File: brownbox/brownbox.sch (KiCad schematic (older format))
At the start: 341 parts, among them J1 Rifle Connector - C7-205, J2 12-Pin Cinch Jones Expansion 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, J3 Jumper, Q1 2N5134, Q10 2N5134, Q11 2N5133, Q12 2N5134, Q13 2N5134, Q14 2N5134, Q15 2N5133, Q16 2N5134, Q17 2N5134, Q18 2N5134, Q19 2N5133, Q2 2N5139, Q20 2N5134, Q21 2N5133, Q22 2N5139, Q23 2N5133, Q24 2N5139, Q25 2N5133, Q26 2N5139, Q27 2N5133, Q28 2N5139, Q29 2N5134, Q3 2N5134, Q30 2N5134, Q31 2N5133, Q32 2N5133, Q33 2N5133, Q34 2N5133, Q35 2N5134, Q36 2N5134, Q37 2N5133, Q38 2N5133, Q39 2N5133, Q4 2N5139, Q40 2N5139, Q41 2N5139, Q42 2N5133, Q43 2N5139, Q44 2N5133, Q45 2N5133, Q46 2N5133, Q5 2N5134, Q6 2N5134, Q7 2N5133, Q8 2N5134, Q9 2N5134, T1 CF104 core, #22 wire, X1 3.579545Mhz

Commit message: More small fixes
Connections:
- net S12A1 is gone; now on net VCC: S12.A1
- net S8B3 is gone; now on net S8C3: S8.C3
- net D: now also S15.B2
- net S15C2: now also S15.C2
- net S15D2: now also S15.D2
- net S16A1: no longer S16.B1
- net S16A2: no longer S16.B2
- net S16B1: now also S16.B1
- net S16B2: now also S16.B2
- net S10A1: no longer names the net of S10.A1
- net S10A2: no longer names the net of S10.A2
- net S10A3: no longer names the net of S10.A3
- net S12A2: no longer names the net of S12.A2
- net S5A2: no longer names the net of S5.A2
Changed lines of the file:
@@
 Text GLabel 15450 10850 0    50   Input ~ 0
 S4A1
-Text GLabel 17200 10750 2    50   Input ~ 0
-S5A2
-Wire Wire Line
-	17200 10750 17100 10750
 Text GLabel 19600 10750 2    50   Input ~ 0
 S7A2
@@
 Wire Wire Line
 	12400 12700 12300 12700
-Text GLabel 13600 12700 2    50   Input ~ 0
-S10A2
-Wire Wire Line
-	13600 12700 13500 12700
-Text GLabel 13600 12900 2    50   Input ~ 0
-S10A3
-Wire Wire Line
-	13600 12900 13500 12900
-Text GLabel 13050 12800 0    50   Input ~ 0
-S10A1
-Wire Wire Line
-	13050 12800 13100 12800
-Wire Wire Line
-	14800 12700 14700 12700
 Text GLabel 14800 12900 2    50   Input ~ 0
 S11A3
 Wire Wire Line
 	14800 12900 14700 12900
-Text GLabel 16000 12700 2    50   Input ~ 0
-S12A2
-Wire Wire Line
-	16000 12700 15900 12700
 Text GLabel 16000 12900 2    50   Input ~ 0
 S12A3
 Wire Wire Line
 	16000 12900 15900 12900
-Text GLabel 15450 12800 0    50   Input ~ 0
-S12A1
-Wire Wire Line
-	15450 12800 15500 12800
 Text GLabel 19600 12700 2    50   Input ~ 0
 S15A2
@@
 	20750 10950 20700 10950
 Text GLabel 20800 11750 2    50   Input ~ 0
-S8B3
+S8C3
 Wire Wire Line
 	20800 11750 20700 11750
@@
 S16B3
 Text GLabel 20250 13200 0    50   Input ~ 0
-S16A1
+S16B1
 Wire Wire Line
 	20250 13200 20300 13200
@@
 	20800 13300 20700 13300
 Text GLabel 20800 13100 2    50   Input ~ 0
-S16A2
+S16B2
 Wire Wire Line
 	20800 13100 20700 13100
@@
 	-1   0    0    1
 $EndComp
+$Comp
+L power:VCC #PWR0204
+U 1 1 60BBF6BF
+P 15200 12750
+F 0 "#PWR0204" H 15200 12600 50  0001 C CNN
+F 1 "VCC" H 15215 12923 50  0000 C CNN
+F 2 "" H 15200 12750 50  0001 C CNN
+F 3 "" H 15200 12750 50  0001 C CNN
+	1    15200 12750
+	-1   0    0    -1
+$EndComp
+Wire Wire Line
+	15200 12750 15200 12800
+Wire Wire Line
+	15200 12800 15500 12800
+Wire Wire Line
+	19600 13500 19500 13500
+Wire Wire Line
+	19600 13100 19500 13100
+Wire Wire Line
+	19600 13900 19500 13900
 $EndSCHEMATC

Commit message: Placed NCs, more fixes, Electrical Rules Check makes sense now
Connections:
- net F': now also S9.C2
- net S7B1: no longer RV4.2, RV4.3
- net S9B1: now reaches S9.B1
- net S9B1: now also RV4.2, RV4.3
- net S4A1: no longer names the net of S2.B2, S4.A1
- no-connect marks 0 -> 113
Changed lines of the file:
@@
 S7A2
 Text GLabel 10200 3000 2    50   Input ~ 0
-S7B1
+S9B1
 Wire Wire Line
 	10200 3000 10100 3000
@@
 	7350 15750 7250 15750
 Wire Wire Line
-	7650 15750 7700 15750
-Wire Wire Line
 	9350 14650 9350 14750
 $Comp
@@
 Wire Wire Line
 	16000 10950 15900 10950
-Text GLabel 15450 10850 0    50   Input ~ 0
-S4A1
 Text GLabel 19600 10750 2    50   Input ~ 0
 S7A2
@@
 	13500 12150 13600 12150
 Wire Wire Line
-	15450 10850 15500 10850
-Connection ~ 15500 10850
-Wire Wire Line
 	13550 11850 16350 11850
 Wire Wire Line
@@
 Wire Wire Line
 	19600 13900 19500 13900
+NoConn ~ 13100 14000
+NoConn ~ 13500 13900
+NoConn ~ 13500 14100
+NoConn ~ 13500 13700
+NoConn ~ 13500 13500
+NoConn ~ 13500 13300
+NoConn ~ 13500 13100
+NoConn ~ 13500 12900
+NoConn ~ 13500 12700
+NoConn ~ 13100 12800
+NoConn ~ 13100 13200
+NoConn ~ 13100 13600
+NoConn ~ 11900 11650
+NoConn ~ 12300 11550
+NoConn ~ 12300 11750
+NoConn ~ 12300 11950
+NoConn ~ 12300 12150
+NoConn ~ 11900 12050
+NoConn ~ 14700 11550
+NoConn ~ 14700 11350
+NoConn ~ 14300 11650
+NoConn ~ 14700 11750
+NoConn ~ 14700 11950
+NoConn ~ 14300 12050
+NoConn ~ 14700 12150
+NoConn ~ 15900 11150
+NoConn ~ 15900 11350
+NoConn ~ 15500 11250
+NoConn ~ 15900 11550
+NoConn ~ 15500 11650
+NoConn ~ 15900 11750
+NoConn ~ 15900 11950
+NoConn ~ 15500 12050
+NoConn ~ 15900 12150
+NoConn ~ 16700 11250
+NoConn ~ 17100 11150
+NoConn ~ 17100 11350
+NoConn ~ 17100 11550
+NoConn ~ 17100 11750
+NoConn ~ 16700 11650
+NoConn ~ 17100 11950
+NoConn ~ 17100 12150
+NoConn ~ 16700 12050
+NoConn ~ 18300 11150
+NoConn ~ 18300 11350
+NoConn ~ 17900 11250
+NoConn ~ 18300 11550
+NoConn ~ 18300 11750
+NoConn ~ 17900 11650
+NoConn ~ 18300 12150
+NoConn ~ 17900 12050
+NoConn ~ 19500 11550
+NoConn ~ 19500 11750
+NoConn ~ 19100 11650
+NoConn ~ 19500 11950
+NoConn ~ 19500 12150
+NoConn ~ 19100 12050
+NoConn ~ 20700 11950
+NoConn ~ 20700 12150
+NoConn ~ 20300 12050
+NoConn ~ 12300 12900
+NoConn ~ 12300 13900
+NoConn ~ 14700 13100
+NoConn ~ 15900 13300
+NoConn ~ 15900 13100
+NoConn ~ 15500 13200
+NoConn ~ 15900 13500
+NoConn ~ 15900 13700
+NoConn ~ 15500 13600
+NoConn ~ 15900 13900
+NoConn ~ 15900 14100
+NoConn ~ 15500 14000
+NoConn ~ 15900 12700
+NoConn ~ 17100 12700
+NoConn ~ 17100 12900
+NoConn ~ 17100 13100
+NoConn ~ 17100 13300
+NoConn ~ 17100 13500
+NoConn ~ 17100 13700
+NoConn ~ 17100 13900
+NoConn ~ 17100 14100
+NoConn ~ 16700 14000
+NoConn ~ 16700 13600
+NoConn ~ 16700 13200
+NoConn ~ 16700 12800
+NoConn ~ 18300 12700
+NoConn ~ 18300 12900
+NoConn ~ 18300 11950
+Wire Wire Line
+	7650 15750 7700 15750
+NoConn ~ 18300 13100
+NoConn ~ 18300 13300
+NoConn ~ 18300 13500
+NoConn ~ 18300 13700
+NoConn ~ 18300 13900
+NoConn ~ 18300 14100
+NoConn ~ 17900 14000
+NoConn ~ 17900 13600
+NoConn ~ 17900 13200
+NoConn ~ 17900 12800
+NoConn ~ 20700 13500
+NoConn ~ 20700 13700
+NoConn ~ 20700 13900
+NoConn ~ 20700 14100
+NoConn ~ 20300 14000
+NoConn ~ 20300 13600
+NoConn ~ 12300 11350
+NoConn ~ 17100 10750
+NoConn ~ 20700 11550
+NoConn ~ 18300 10750
+Wire Wire Line
+	12400 13500 12300 13500
+Text GLabel 11800 13200 0    50   Input ~ 0
+S9B1
+Wire Wire Line
+	11800 13200 11900 13200
+NoConn ~ 14700 12700
+NoConn ~ 17200 8650
+NoConn ~ 17600 8650
+NoConn ~ 17950 8650
+NoConn ~ 18350 8650
 $EndSCHEMATC

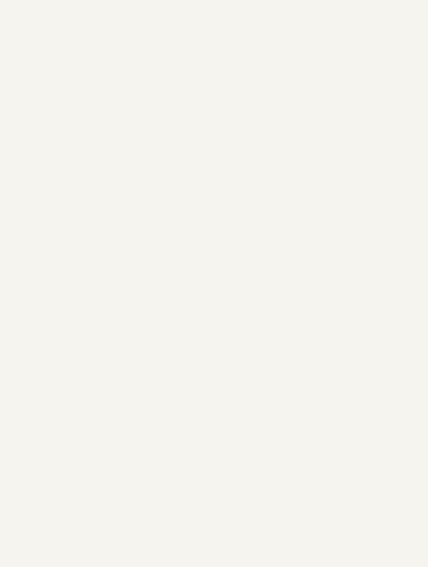
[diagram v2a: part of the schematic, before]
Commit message: Start adding footprints
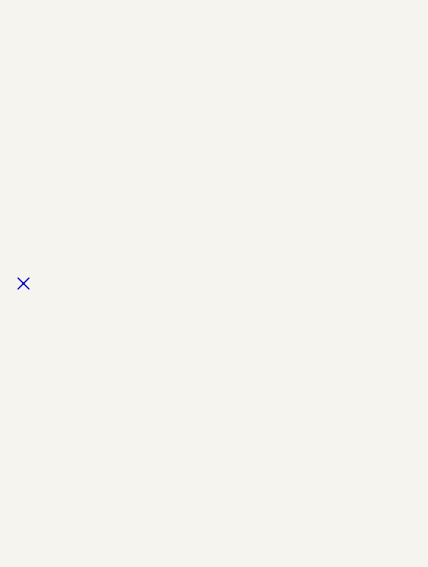
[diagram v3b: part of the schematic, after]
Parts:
- BT1, BT2, J3: footprint (none) -> Connector_PinHeader_2.54mm:PinHeader_1x02_P2.54mm_Vertical
- J1: footprint (none) -> Connector_IDC:IDC-Header_2x04_P2.54mm_Vertical
- J2: footprint (none) -> Connector_IDC:IDC-Header_2x06_P2.54mm_Vertical
- R1, R10, R100, R101, R102, R103, R104, R106, R107, R108, R109, R11, R110, R111, R112, R113, R114, R115, R116, R117, R118, R119, R12, R120, R121, R122, R123, R124, R125, R126, R127, R128, R129, R13, R130, R131, R132, R133, R134, R135, R136, R137, R138, R139, R14, R140, R141, R142, R143, R144, R145, R146, R147, R148, R15, R16, R17, R18, R19, R2, R20, R21, R22, R23, R24, R25, R26, R27, R28, R29, R3, R30, R31, R32, R33, R34, R35, R36, R37, R38, R39, R4, R40, R41, R42, R43, R44, R45, R46, R47, R48, R49, R5, R50, R51, R52, R53, R54, R55, R56, R57, R58, R59, R6, R60, R61, R62, R63, R64, R65, R66, R67, R68, R69, R7, R70, R71, R72, R73, R74, R75, R76, R77, R78, R79, R8, R80, R81, R82, R83, R84, R85, R86, R87, R88, R89, R9, R90, R91, R92, R93, R94, R95, R96, R97, R98, R99: footprint (none) -> Resistor_THT:R_Axial_DIN0207_L6.3mm_D2.5mm_P7.62mm_Horizontal
- RV1, RV2, RV3, RV4, RV5, RV8, RV9: footprint (none) -> Potentiometer_THT:Potentiometer_Bourns_3266W_Vertical
- RV10, RV11, RV12, RV13, RV6, RV7: footprint (none) -> Potentiometer_THT:Potentiometer_Piher_PT-15-H01_Horizontal
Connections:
- no-connect marks 113 -> 114
